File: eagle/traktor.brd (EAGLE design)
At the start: 91.1 x 36.2 mm, 20 parts

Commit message: secound version
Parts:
- removed D9, U$5, U$7: I_O_PIN, traktor:I_O_PIN
- added 5V, 5V1, A3, A7, D1, D13, D6, GND_, GND_1: I_O_PIN, traktor:I_O_PIN
- added LED1: (no value), led:LED5MM
- added R6: (no value), resistor:R0805
- R3, R4, R5: value 6K8 -> (none); device resistor:R0603 -> resistor:R0805
- U$4, U$6: value I_O_PIN -> BUTTON; device traktor:I_O_PIN -> traktor:BUTTON
- moved R1 63.9 mm to (10.5, 30.5), flipped to the bottom
- moved R2 60.4 mm to (12.7, 30.5), flipped to the bottom, turned to 90 degrees
- moved U$3 47.2 mm to (60.3, 25.1), turned to 180 degrees
- moved R4 29.7 mm to (107.0, 28.6), flipped to the bottom
- moved R5 25.9 mm to (108.9, 19.1), flipped to the bottom, turned to 180 degrees
- moved U$1 25.7 mm to (21.6, 18.4), turned to 0 degrees
- moved R3 24.1 mm to (107.0, 23.5), flipped to the bottom, turned to 180 degrees
- moved U$4 21.5 mm to (102.2, 13.7), turned to 270 degrees
- moved U$6 20.2 mm to (102.2, 28.6), turned to 270 degrees
- moved SCL 17.0 mm to (54.6, 40.6)
- moved VIN 17.0 mm to (44.5, 40.6)
- moved A0 12.7 mm to (69.8, 40.6)
- moved A1 12.7 mm to (64.8, 40.6)
- moved A2 12.7 mm to (59.7, 40.6)
- moved GND 9.16 mm to (39.4, 40.6)
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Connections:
- new net GND1: GND_1.P$1, LED1.K, R5.2
- new net N$20: 5V1.P$1, R4.2, U$6.A, U$6.AA
- new net N$21: LED1.A, R6.1
- new net N$22: D1.P$1, R6.2
- new net N$9: A7.P$1, U$1.A7
- net 5V: now also 5V.P$1; no longer R3.2, R4.2, R5.2
- net GND: now also GND_.P$1; no longer U$7.P$1
- net N$16: now also D13.P$1, U$1.D13; no longer D9.P$1, U$1.D9
- net N$17: now also D6.P$1, U$1.D6; no longer R4.1, U$1.D8, U$4.P$1
- net N$18: now also A3.P$1, R3.2, U$4.B, U$4.BB; no longer U$1.D7, U$5.P$1
- net N$19: now also R4.1, U$4.A, U$4.AA, U$6.B, U$6.BB; no longer U$1.D6, U$6.P$1
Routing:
- net N$14: track 11.8 -> 100.2 mm
- net N$15: track 10.8 -> 98.2 mm
- net N$1: track 11.2 -> 96.0 mm
- net N$9: track 0.00 -> 61.0 mm, vias 0 -> 2
- net N$16: track 49.4 -> 106.7 mm
- net 5V: track 174.1 -> 222.1 mm
- net N$17: track 39.5 -> 86.7 mm, vias 0 -> 2
- net GND: track 190.8 -> 156.2 mm
- net N$2: track 35.5 -> 69.3 mm
- net N$20: track 0.00 -> 31.5 mm
- net N$19: track 48.1 -> 19.8 mm
- net GND1: track 0.00 -> 26.6 mm
- net N$13: track 10.8 -> 34.9 mm
- net N$18: track 46.9 -> 24.1 mm
- net N$12: track 53.2 -> 75.6 mm
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- added copper zone on layer 16, net GND
- added copper zone on layer 16, net GND1
- removed copper zone on layer 1, net GND
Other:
- board size 91.1 x 36.2 mm -> 96.6 x 44.4 mm

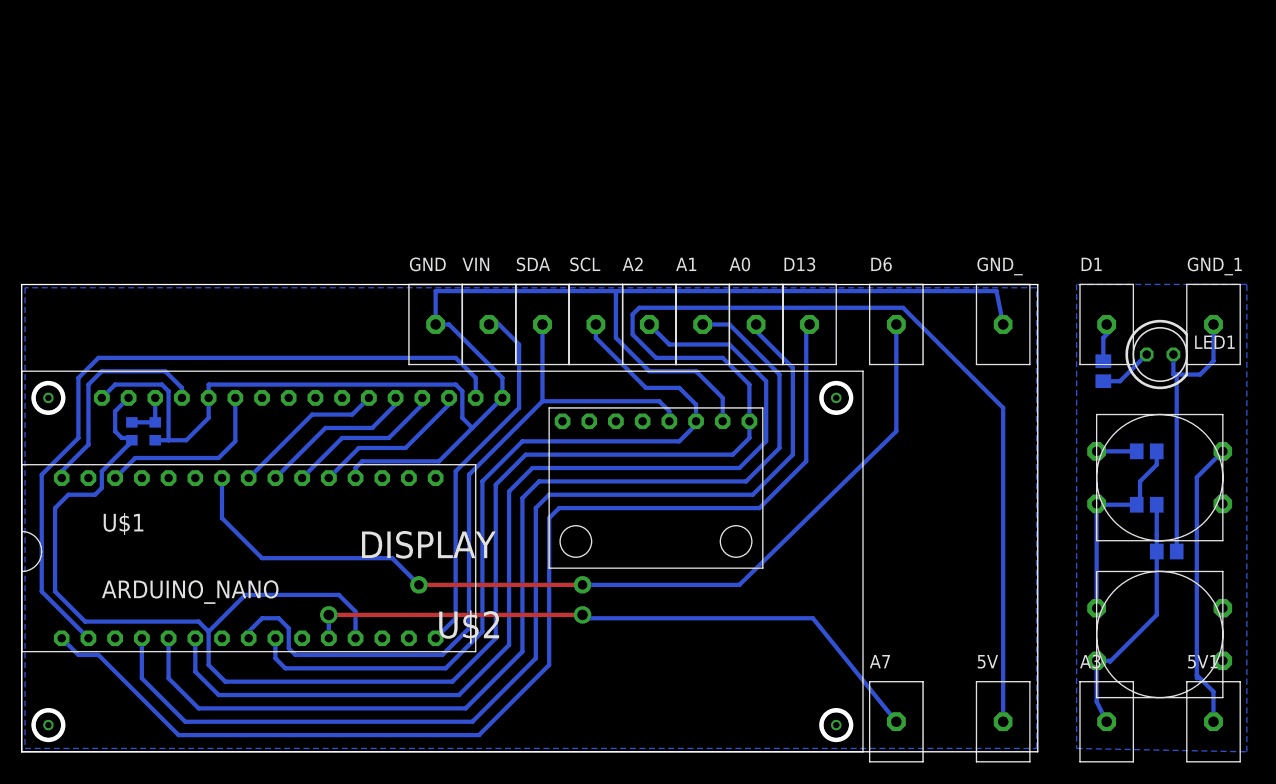
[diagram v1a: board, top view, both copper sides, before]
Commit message: 5V Instead Of D13
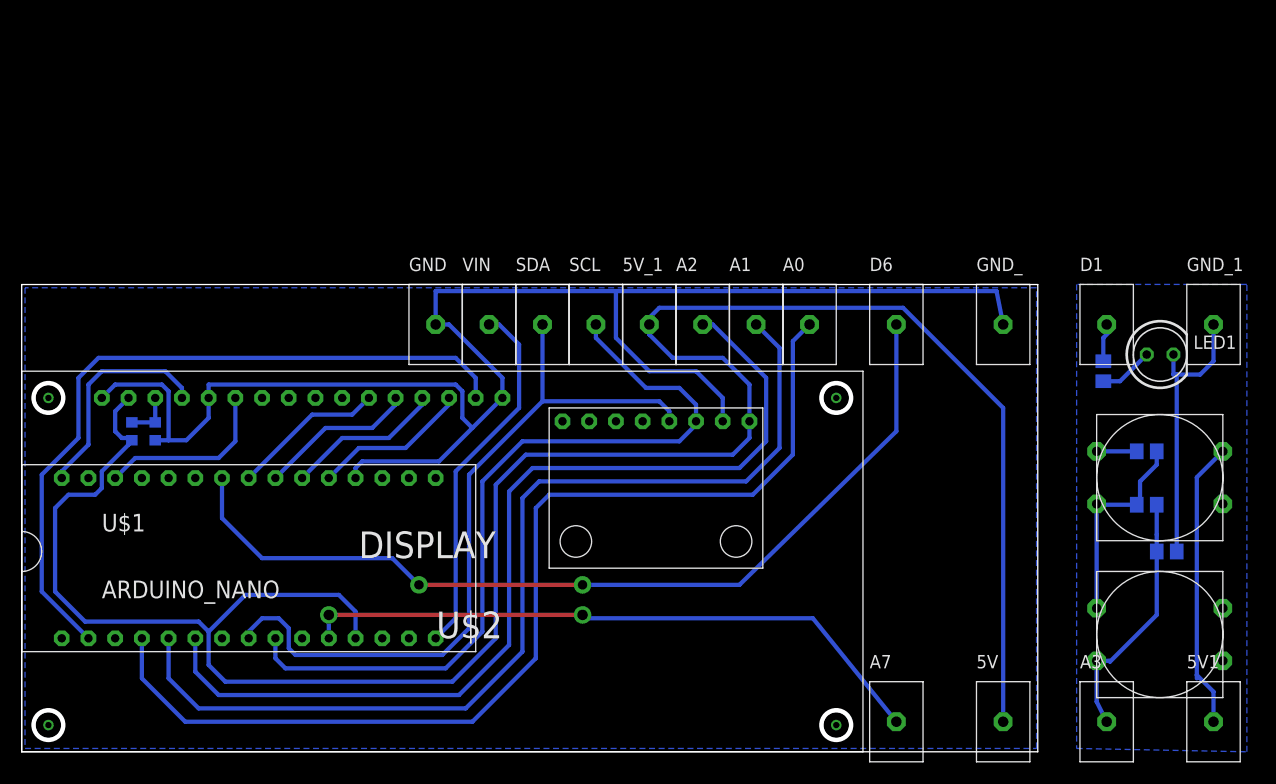
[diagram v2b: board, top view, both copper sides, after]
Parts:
- removed D13: I_O_PIN, traktor:I_O_PIN
- added 5V_1: I_O_PIN, traktor:I_O_PIN
- moved A0 5.08 mm to (74.9, 40.6)
- moved A1 5.08 mm to (69.8, 40.6)
- moved A2 5.08 mm to (64.8, 40.6)
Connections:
- removed net N$16: D13.P$1, U$1.D13
- net 5V: now also 5V_1.P$1
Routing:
- net N$16: track 106.7 -> 0.00 mm
- net N$1: track 96.0 -> 91.1 mm
- net N$15: track 98.2 -> 94.6 mm
- net 5V: track 222.1 -> 218.7 mm
- net N$14: track 100.2 -> 99.4 mm

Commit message: added 7805
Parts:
- added C1: 330 nF, resistor:C0805
- added C2: 100nF, resistor:C0805
- added D2: 1N4004, diode:DO41-10
- added DC1: R-78C5.0-1.0, dc-dc-converter:SIP3
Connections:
- new net VIN: D2.A, VIN.P$1
- net 5V: now also C2.1, DC1.3
- net GND: now also C1.2, C2.2, DC1.2, U$2.D0, U$2.D1, U$2.D2, U$2.D3
- net N$13: now also C1.1, D2.C, DC1.1; no longer U$1.VIN, VIN.P$1
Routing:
- net GND: track 156.2 -> 220.6 mm
- net VIN: track 0.00 -> 58.8 mm, vias 0 -> 2
- net N$13: track 34.9 -> 9.15 mm
- net 5V: track 218.7 -> 235.0 mm
- net N$7: track 17.0 -> 15.1 mm
- net N$17: track 86.7 -> 85.0 mm
- net N$2: track 69.3 -> 69.8 mm

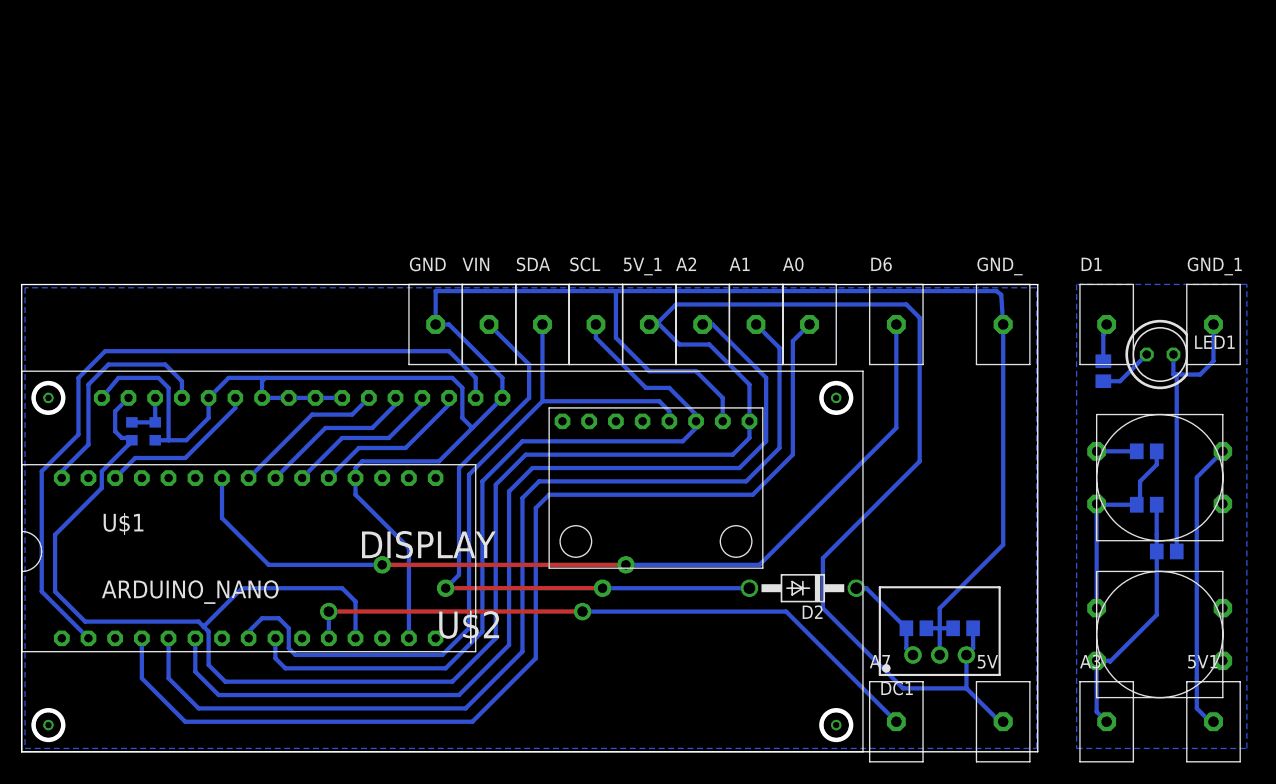
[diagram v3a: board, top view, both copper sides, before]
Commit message: changes for external MPU and LED bar - PCB redesigned to two layer one
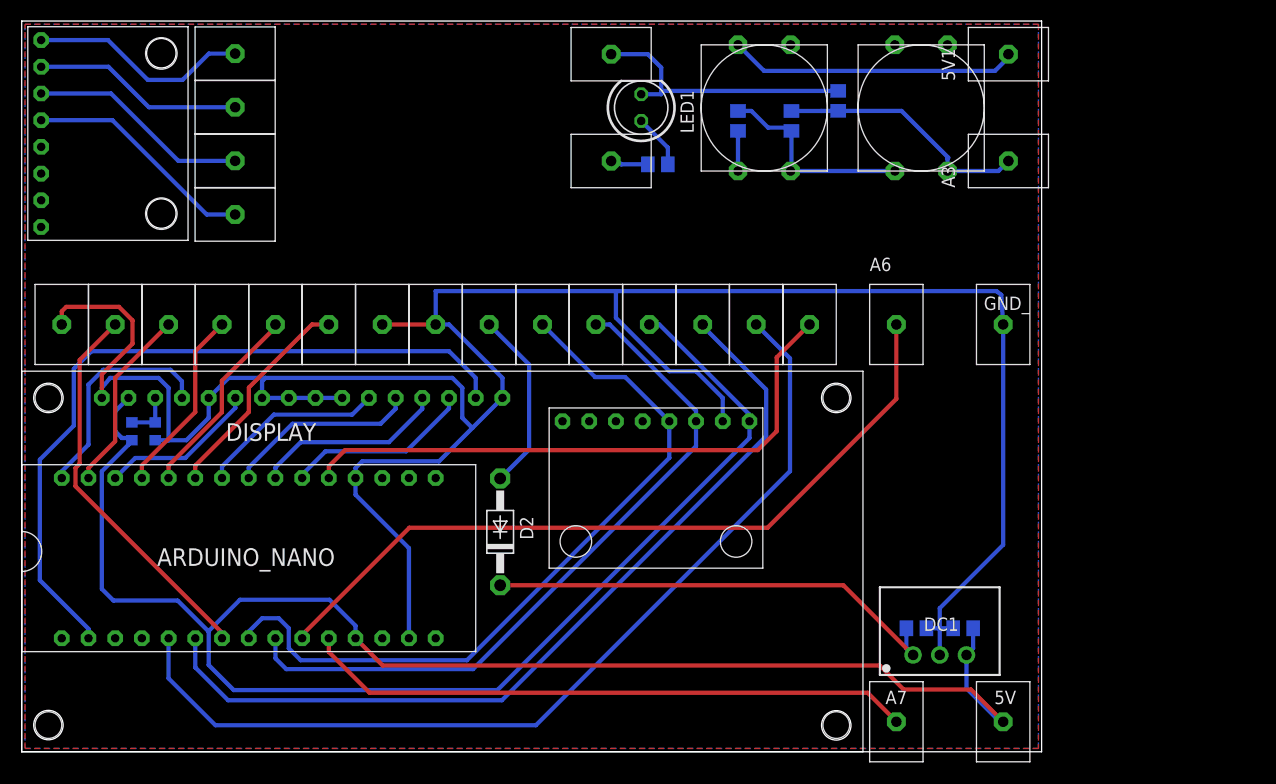
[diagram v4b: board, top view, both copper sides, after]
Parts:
- added GND., LED_1, LED_2, LED_3, LED_4, LED_GND, PIEZO+, PIEZO-, SCL., SDA., VCC.: I_O_PIN, traktor:I_O_PIN
- added U$5: GYRO, traktor:GYRO
- moved 5V1 66.4 mm to (93.8, 66.3), turned to 90 degrees
- moved GND_1 62.8 mm to (56.1, 66.3), turned to 90 degrees
- moved LED1 54.7 mm to (58.9, 61.3), turned to 90 degrees
- moved A3 54.1 mm to (93.8, 56.2), turned to 90 degrees
- moved R5 53.0 mm to (77.7, 61.9), turned to 90 degrees
- moved R4 50.0 mm to (68.1, 60.0), turned to 270 degrees
- moved R3 49.7 mm to (73.2, 60.0), turned to 90 degrees
- moved D1 49.6 mm to (56.1, 56.2), turned to 90 degrees
- moved R6 46.7 mm to (60.5, 55.9), turned to 0 degrees
- moved U$4 45.8 mm to (83.0, 55.2), turned to 0 degrees
- moved U$6 43.3 mm to (68.1, 55.2), turned to 0 degrees
- moved D2 29.3 mm to (45.5, 20.9), turned to 90 degrees
- renumbered A0 to D2_, D6 to A6
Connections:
- new net N$16: PIEZO+.P$1, U$1.A3
- new net N$27: LED_1.P$1, U$1.D11
- new net N$28: LED_2.P$1, U$1.D9
- new net N$29: LED_3.P$1, U$1.D8
- new net N$30: LED_4.P$1, U$1.D7
- new net N$31: U$5.VCC, VCC..P$1
- new net N$32: GND..P$1, U$5.GND
- new net N$33: SCL..P$1, U$5.SCL
- new net N$34: SDA..P$1, U$5.SDA
- net GND: now also LED_GND.P$1, PIEZO-.P$1
- net N$14: now also U$1.D2; no longer U$1.A0
- net N$17: now also U$1.A6; no longer U$1.D6
- net N$3: now also U$1.D3; no longer U$1.D2
- net N$4: now also U$1.D4; no longer U$1.D3
- net N$5: now also U$1.D5; no longer U$1.D4
- net N$6: now also U$1.D6; no longer U$1.D5
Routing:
- net N$14: track 99.4 -> 56.5 mm
- net VIN: track 58.8 -> 17.4 mm, vias 2 -> 0
- net N$16: track 0.00 -> 37.2 mm
- net N$13: track 9.15 -> 44.8 mm
- net 5V: track 235.0 -> 206.7 mm
- net N$34: track 0.00 -> 22.2 mm
- net GND: track 220.6 -> 242.4 mm
- net N$33: track 0.00 -> 21.1 mm
- net N$31: track 0.00 -> 21.1 mm
- net N$30: track 0.00 -> 20.8 mm
- net N$32: track 0.00 -> 20.0 mm
- net N$29: track 0.00 -> 18.8 mm
- net N$28: track 0.00 -> 17.8 mm
- net N$27: track 0.00 -> 17.8 mm
- net N$17: track 85.0 -> 73.2 mm, vias 2 -> 0
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- added copper zone on layer 1, net GND
- removed copper zone on layer 16, net GND1
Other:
- board size 96.6 x 44.4 mm -> 97 x 69.5 mm
- board text added: "TJ-25 v2"

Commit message: version 2023-05-04
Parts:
- R3, R5: value (none) -> 10k
- R4: value (none) -> 4k7
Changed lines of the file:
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@@
 <layer number="25" name="tNames" color="7" fill="1" visible="yes" active="yes"/>
 <layer number="26" name="bNames" color="7" fill="1" visible="yes" active="yes"/>
-<layer number="27" name="tValues" color="7" fill="1" visible="yes" active="yes"/>
-<layer number="28" name="bValues" color="7" fill="1" visible="yes" active="yes"/>
-<layer number="29" name="tStop" color="7" fill="3" visible="yes" active="yes"/>
-<layer number="30" name="bStop" color="7" fill="6" visible="yes" active="yes"/>
-<layer number="31" name="tCream" color="7" fill="4" visible="yes" active="yes"/>
-<layer number="32" name="bCream" color="7" fill="5" visible="yes" active="yes"/>
-<layer number="33" name="tFinish" color="6" fill="3" visible="yes" active="yes"/>
-<layer number="34" name="bFinish" color="6" fill="6" visible="yes" active="yes"/>
-<layer number="35" name="tGlue" color="7" fill="4" visible="yes" active="yes"/>
-<layer number="36" name="bGlue" color="7" fill="5" visible="yes" active="yes"/>
-<layer number="37" name="tTest" color="7" fill="1" visible="yes" active="yes"/>
-<layer number="38" name="bTest" color="7" fill="1" visible="yes" active="yes"/>
+<layer number="27" name="tValues" color="7" fill="1" visible="no" active="yes"/>
+<layer number="28" name="bValues" color="7" fill="1" visible="no" active="yes"/>
+<layer number="29" name="tStop" color="7" fill="3" visible="no" active="yes"/>
+<layer number="30" name="bStop" color="7" fill="6" visible="no" active="yes"/>
+<layer number="31" name="tCream" color="7" fill="4" visible="no" active="yes"/>
+<layer number="32" name="bCream" color="7" fill="5" visible="no" active="yes"/>
+<layer number="33" name="tFinish" color="6" fill="3" visible="no" active="yes"/>
+<layer number="34" name="bFinish" color="6" fill="6" visible="no" active="yes"/>
+<layer number="35" name="tGlue" color="7" fill="4" visible="no" active="yes"/>
+<layer number="36" name="bGlue" color="7" fill="5" visible="no" active="yes"/>
+<layer number="37" name="tTest" color="7" fill="1" visible="no" active="yes"/>
+<layer number="38" name="bTest" color="7" fill="1" visible="no" active="yes"/>
 <layer number="39" name="tKeepout" color="4" fill="11" visible="yes" active="yes"/>
 <layer number="40" name="bKeepout" color="1" fill="11" visible="yes" active="yes"/>
 <layer number="41" name="tRestrict" color="4" fill="10" visible="yes" active="yes"/>
 <layer number="42" name="bRestrict" color="1" fill="10" visible="yes" active="yes"/>
-<layer number="43" name="vRestrict" color="2" fill="10" visible="yes" active="yes"/>
-<layer number="44" name="Drills" color="7" fill="1" visible="yes" active="yes"/>
-<layer number="45" name="Holes" color="7" fill="1" visible="yes" active="yes"/>
-<layer number="46" name="Milling" color="3" fill="1" visible="yes" active="yes"/>
-<layer number="47" name="Measures" color="7" fill="1" visible="yes" active="yes"/>
-<layer number="48" name="Document" color="7" fill="1" visible="yes" active="yes"/>
-<layer number="49" name="Reference" color="7" fill="1" visible="yes" active="yes"/>
+<layer number="43" name="vRestrict" color="2" fill="10" visible="no" active="yes"/>
+<layer number="44" name="Drills" color="7" fill="1" visible="no" active="yes"/>
+<layer number="45" name="Holes" color="7" fill="1" visible="no" active="yes"/>
+<layer number="46" name="Milling" color="3" fill="1" visible="no" active="yes"/>
+<layer number="47" name="Measures" color="7" fill="1" visible="no" active="yes"/>
+<layer number="48" name="Document" color="7" fill="1" visible="no" active="yes"/>
+<layer number="49" name="Reference" color="7" fill="1" visible="no" active="yes"/>
 <layer number="51" name="tDocu" color="7" fill="1" visible="yes" active="yes"/>
 <layer number="52" name="bDocu" color="7" fill="1" visible="yes" active="yes"/>
@@
 <layer number="98" name="Guide" color="6" fill="1" visible="no" active="no"/>
 <layer number="99" name="SpiceOrder" color="5" fill="1" visible="no" active="no"/>
-<layer number="116" name="centerDrill" color="7" fill="1" visible="yes" active="yes"/>
+<layer number="116" name="centerDrill" color="7" fill="1" visible="no" active="yes"/>
 </layers>
 <board>
@@
 </element>
 <element name="GND_1" library="traktor" package="I_O_PIN" value="I_O_PIN" x="56.06" y="66.3475" smashed="yes" rot="R90"/>
-<element name="R3" library="resistor" package="R0805" value="" x="73.205" y="59.9975" smashed="yes" rot="MR90">
+<element name="R3" library="resistor" package="R0805" value="10k" x="73.205" y="59.9975" smashed="yes" rot="MR90">
 <attribute name="NAME" x="74.275" y="58.9625" size="1.27" layer="26" rot="MR90"/>
 <attribute name="VALUE" x="70.665" y="59.3625" size="1.27" layer="28" rot="MR90"/>
 </element>
-<element name="R4" library="resistor" package="R0805" value="" x="68.125" y="59.9975" smashed="yes" rot="MR270">
+<element name="R4" library="resistor" package="R0805" value="4k7" x="68.125" y="59.9975" smashed="yes" rot="MR270">
 <attribute name="NAME" x="69.145" y="58.9675" size="1.27" layer="26" rot="MR90"/>
 <attribute name="VALUE" x="70.665" y="60.6325" size="1.27" layer="28" rot="MR270"/>
 </element>
-<element name="R5" library="resistor" package="R0805" value="" x="77.65" y="61.9025" smashed="yes" rot="MR90">
+<element name="R5" library="resistor" package="R0805" value="10k" x="77.65" y="61.9025" smashed="yes" rot="MR90">
 <attribute name="NAME" x="78.72" y="60.8675" size="1.27" layer="26" rot="MR90"/>
 <attribute name="VALUE" x="75.11" y="61.2675" size="1.27" layer="28" rot="MR90"/>
